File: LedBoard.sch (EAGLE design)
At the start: 18 parts

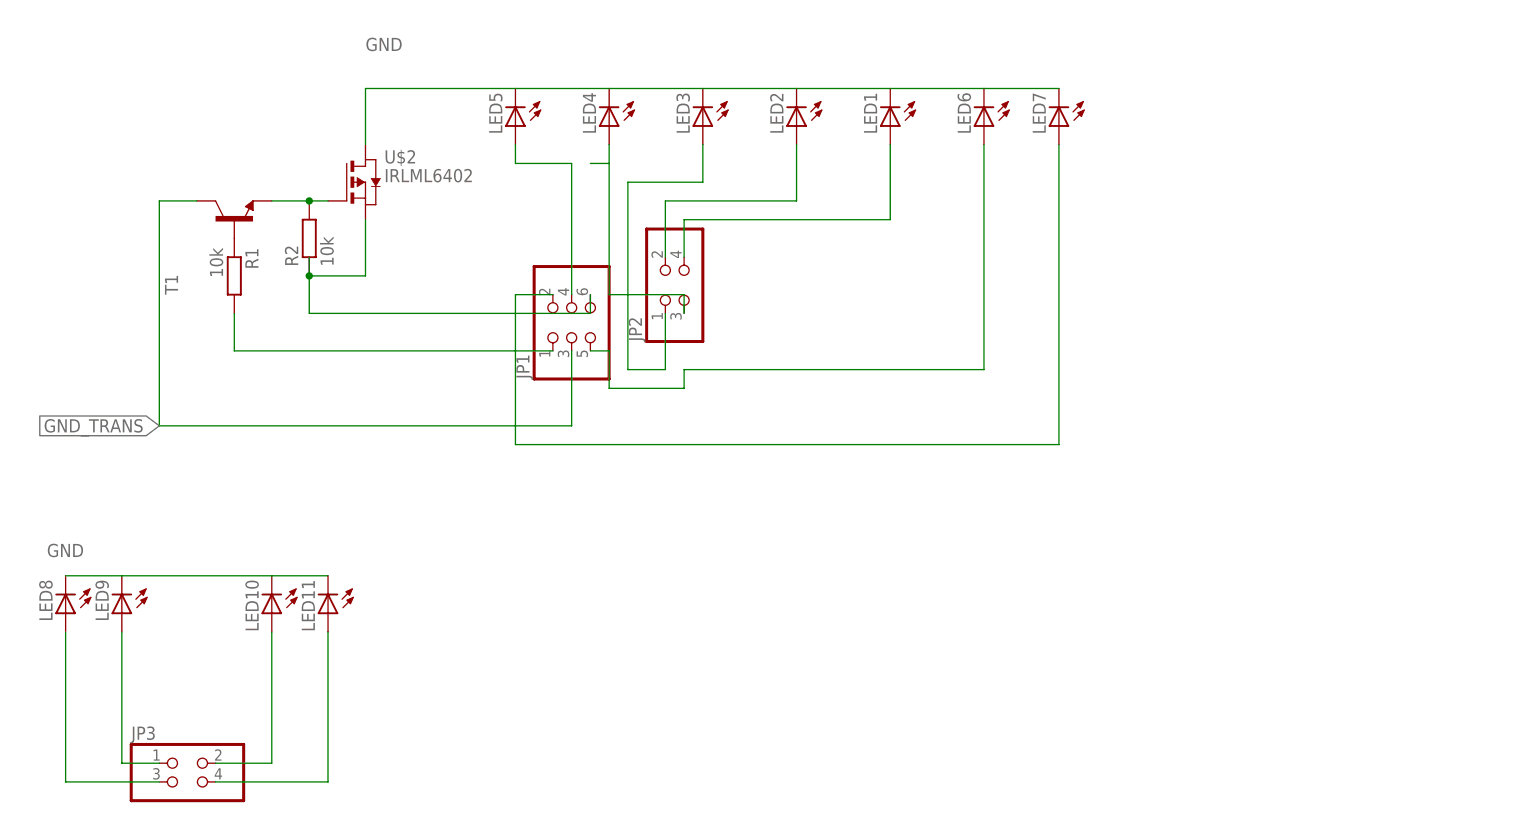
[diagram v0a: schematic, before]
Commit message: Finished Routing an Panelizing
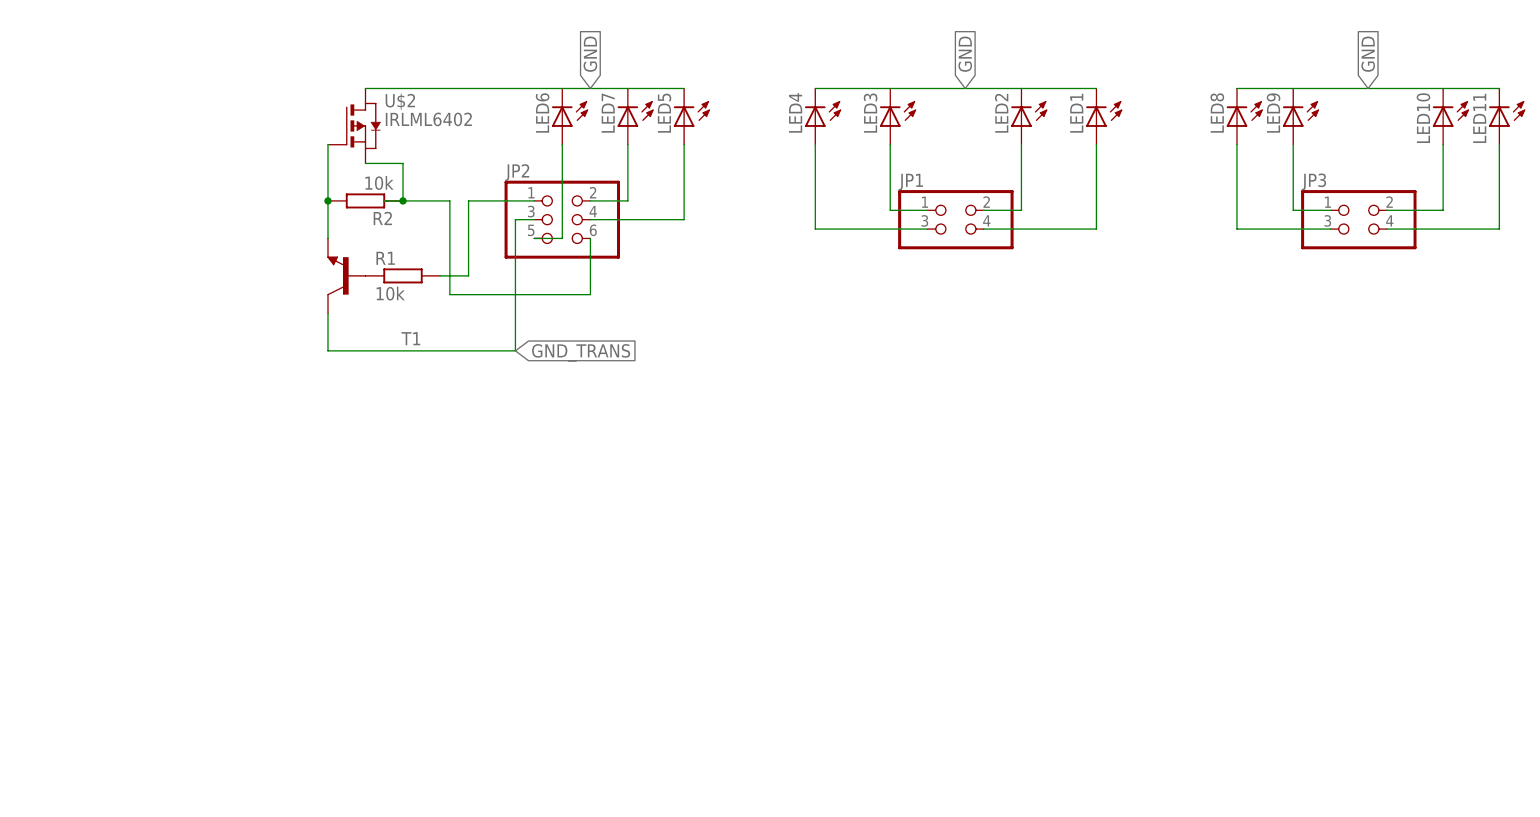
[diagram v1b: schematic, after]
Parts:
- JP1: device pinhead:PINHD-2X3 -> pinhead:PINHD-2X2
- JP2: device pinhead:PINHD-2X2 -> pinhead:PINHD-2X3
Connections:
- net GND_TRANS: now also JP2.3; no longer JP1.3
- net N$1: now also JP1.4; no longer JP2.4
- net N$14: now also JP2.2; no longer JP1.2
- net N$15: now also JP2.1; no longer JP1.1
- net N$3: now also JP1.2; no longer JP2.2
- net N$4: now also JP1.1; no longer JP2.1
- net N$5: now also JP1.3; no longer JP2.3
- net N$6: now also JP2.4; no longer JP1.4
- net N$7: now also JP2.5; no longer JP1.5
- net N$9: now also JP2.6; no longer JP1.6
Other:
- moved on the sheet: JP3, LED1, LED10, LED11, LED2, LED3, LED4, LED5, LED6, LED7, LED8, LED9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

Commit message: Changed tolerances on ledboard and mainboard
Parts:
- renumbered JP1 to J1, JP2 to J2, JP3 to J3, LED1 to L1, LED10 to L10, LED11 to L11, LED2 to L2, LED3 to L3, LED4 to L4, LED5 to L5, LED6 to L6, LED7 to L7, LED8 to L8, LED9 to L9, U$2 to IR
